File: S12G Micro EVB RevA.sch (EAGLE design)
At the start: 35 parts, among them IC1 FT232RL, IC2 MCP1640, J1 JUMPER_2WAY, J2 JUMPER

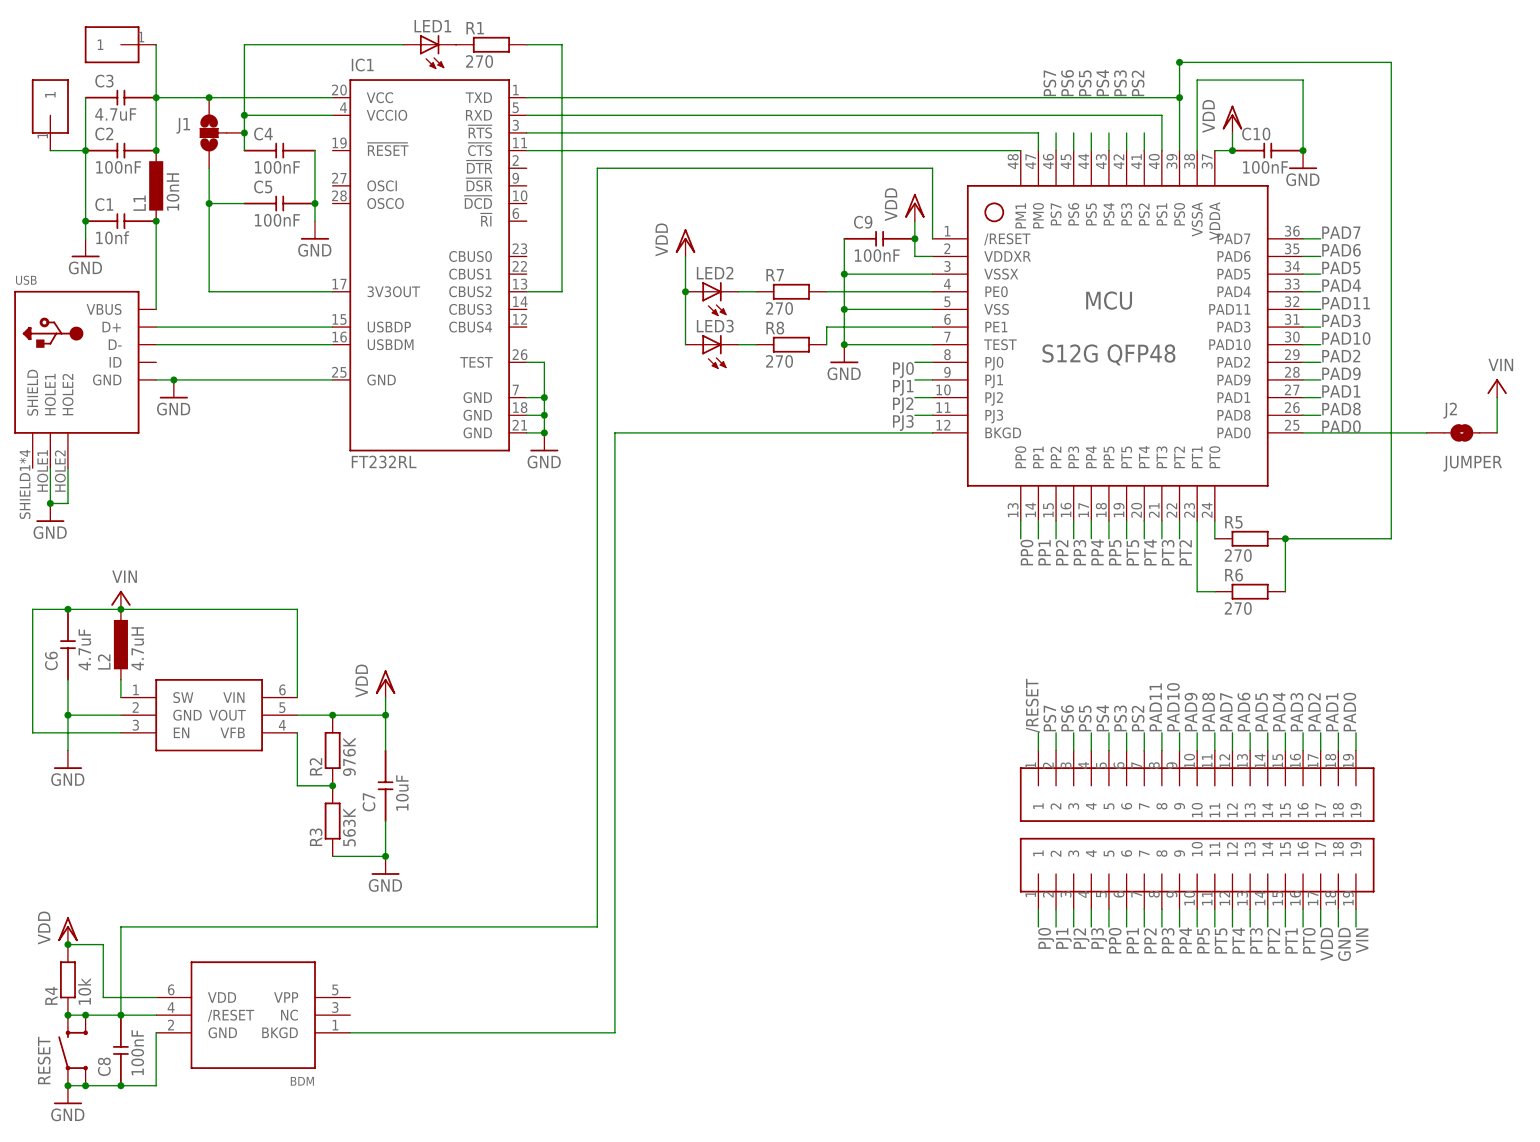
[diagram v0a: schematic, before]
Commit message: added BOM
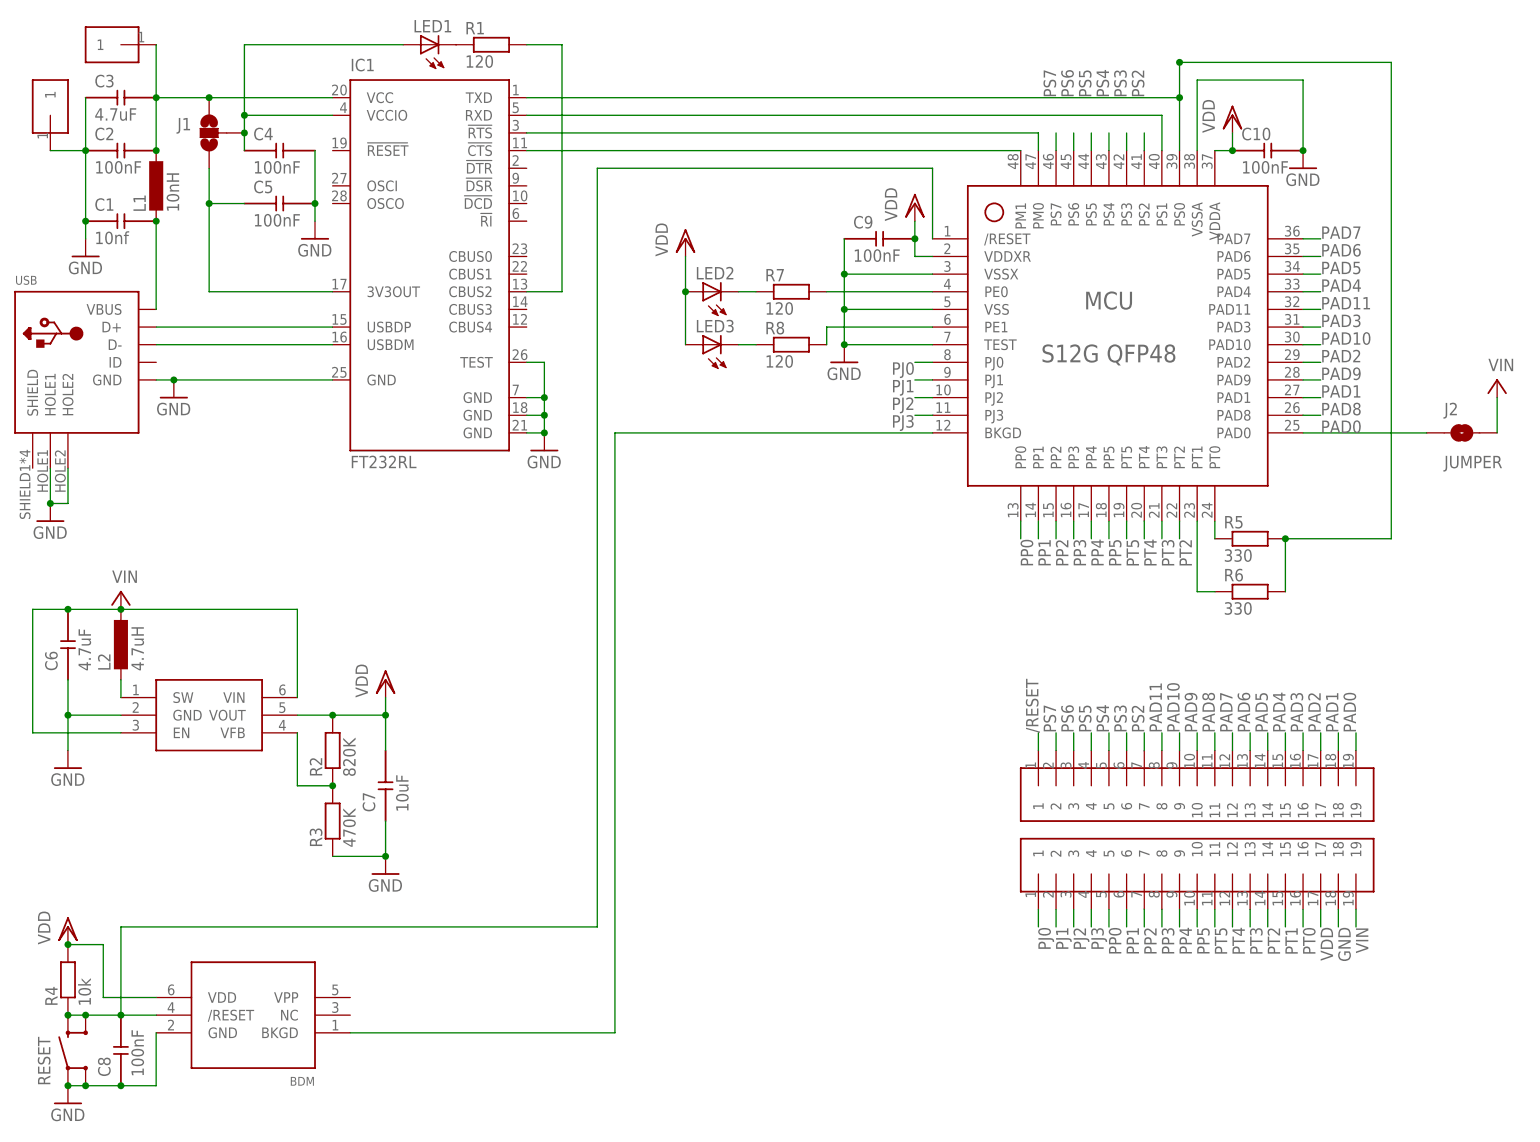
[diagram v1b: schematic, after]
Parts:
- R1, R7, R8: value 270 -> 120
- R2: value 976K -> 820K
- R3: value 563K -> 470K
- R5, R6: value 270 -> 330
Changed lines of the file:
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@@
 <?xml version="1.0" encoding="utf-8"?>
 <!DOCTYPE eagle SYSTEM "eagle.dtd">
-<eagle version="6.0">
+<eagle version="6.1">
 <drawing>
 <settings>
@@
 <part name="GND1" library="supply1" deviceset="GND" device=""/>
 <part name="C1" library="myLibrary" deviceset="C" device="" value="10nf"/>
-<part name="R2" library="myLibrary" deviceset="R" device="" value="976K"/>
+<part name="R2" library="myLibrary" deviceset="R" device="" value="820K"/>
 <part name="GND2" library="supply1" deviceset="GND" device=""/>
 <part name="GND3" library="supply1" deviceset="GND" device=""/>
@@
 <part name="VDD3" library="supply1" deviceset="VDD" device=""/>
 <part name="IC2" library="myLibrary" deviceset="MCP1640" device=""/>
-<part name="R3" library="myLibrary" deviceset="R" device="" value="563K"/>
+<part name="R3" library="myLibrary" deviceset="R" device="" value="470K"/>
 <part name="GND11" library="supply1" deviceset="GND" device=""/>
 <part name="L1" library="myLibrary" deviceset="L" device="0805" value="10nH"/>
@@
 <part name="RESET" library="myLibrary" deviceset="BUTTON" device="" value=""/>
 <part name="LED1" library="myLibrary" deviceset="LED" device="0805" value=""/>
-<part name="R1" library="myLibrary" deviceset="R" device="" value="270"/>
+<part name="R1" library="myLibrary" deviceset="R" device="" value="120"/>
 <part name="C10" library="myLibrary" deviceset="C" device="" value="100nF"/>
-<part name="R5" library="myLibrary" deviceset="R" device="" value="270"/>
-<part name="R6" library="myLibrary" deviceset="R" device="" value="270"/>
+<part name="R5" library="myLibrary" deviceset="R" device="" value="330"/>
+<part name="R6" library="myLibrary" deviceset="R" device="" value="330"/>
 <part name="VIN" library="supply2" deviceset="V+" device="" value="VIN"/>
 <part name="LED2" library="myLibrary" deviceset="LED" device="0805" value=""/>
-<part name="R7" library="myLibrary" deviceset="R" device="" value="270"/>
+<part name="R7" library="myLibrary" deviceset="R" device="" value="120"/>
 <part name="VDD2" library="supply1" deviceset="VDD" device=""/>
 <part name="BOTTOM" library="myLibrary" deviceset="1X19" device=""/>
 <part name="TOP" library="myLibrary" deviceset="1X19" device=""/>
 <part name="LED3" library="myLibrary" deviceset="LED" device="0805" value=""/>
-<part name="R8" library="myLibrary" deviceset="R" device="" value="270"/>
+<part name="R8" library="myLibrary" deviceset="R" device="" value="120"/>
 <part name="GND5" library="supply1" deviceset="GND" device=""/>
 <part name="J2" library="myLibrary" deviceset="JUMPER" device=""/>
